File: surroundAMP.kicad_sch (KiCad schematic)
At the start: 22 parts, among them U1 NJM4580

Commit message: comments added
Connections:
- net OUPUT C L renamed OUTPUT C L
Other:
- note added: "R+L for Center Speaker Power AMP"
- note added: "R-L and L-R for rear speaker Power AMP"
- note added: "Surround Processor for rear speakers"
- note removed: "R+L for Center Speaker"
- note removed: "Surround Effector"
- moved on the sheet: R10, R11, R15, R3, R4

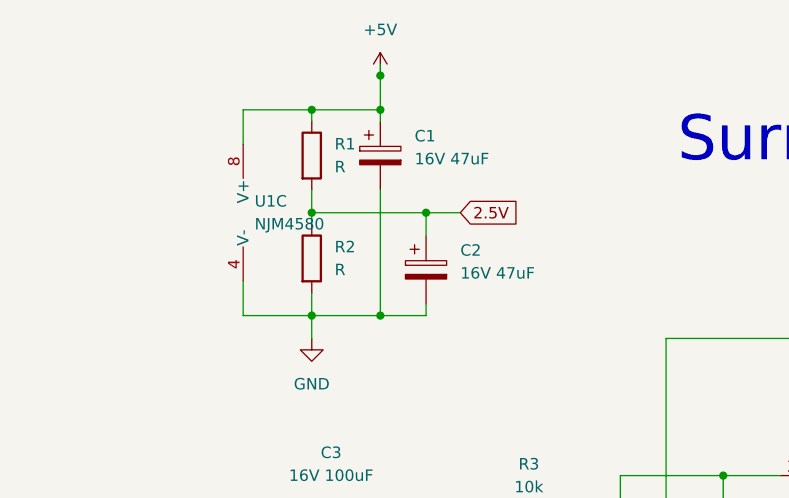
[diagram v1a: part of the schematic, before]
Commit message: resister 4.7k for 2.5V Power supply are specified
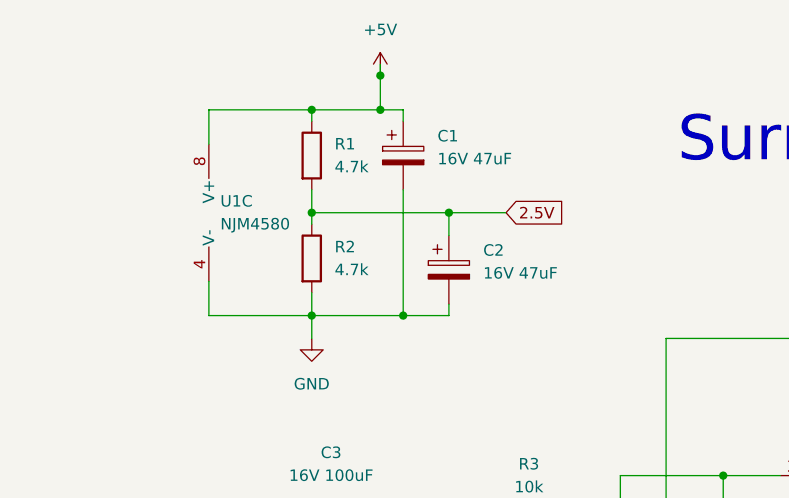
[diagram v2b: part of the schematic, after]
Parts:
- R1, R2: value R -> 4.7k
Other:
- moved on the sheet: C1, C2, U1C
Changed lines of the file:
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@@
   (junction (at 97.79 76.2) (diameter 0) (color 0 0 0 0)
   )
+  (junction (at 68.58 53.34) (diameter 0) (color 0 0 0 0)
+  )
   (junction (at 45.72 181.61) (diameter 0) (color 0 0 0 0)
   )
@@
   (junction (at 52.07 76.2) (diameter 0) (color 0 0 0 0)
   )
-  (junction (at 66.04 53.34) (diameter 0) (color 0 0 0 0)
-  )
   (junction (at 66.04 96.52) (diameter 0) (color 0 0 0 0)
   )
-  (junction (at 71.12 41.91) (diameter 0) (color 0 0 0 0)
-  )
   (junction (at 114.3 161.29) (diameter 0) (color 0 0 0 0)
   )
@@
   (junction (at 58.42 30.48) (diameter 0) (color 0 0 0 0)
   )
+  (junction (at 73.66 41.91) (diameter 0) (color 0 0 0 0)
+  )
   (junction (at 104.14 71.12) (diameter 0) (color 0 0 0 0)
   )
@@
     (stroke (width 0) (type default))
   )
-  (wire (pts (xy 66.04 53.34) (xy 71.12 53.34))
-    (stroke (width 0) (type default))
-  )
   (wire (pts (xy 46.99 96.52) (xy 46.99 172.72))
     (stroke (width 0) (type default))
@@
     (stroke (width 0) (type default))
   )
-  (wire (pts (xy 58.42 53.34) (xy 50.8 53.34))
+  (wire (pts (xy 58.42 53.34) (xy 46.99 53.34))
     (stroke (width 0) (type default))
   )
@@
     (stroke (width 0) (type default))
   )
-  (wire (pts (xy 66.04 31.75) (xy 66.04 30.48))
+  (wire (pts (xy 68.58 31.75) (xy 68.58 30.48))
     (stroke (width 0) (type default))
   )
@@
     (stroke (width 0) (type default))
   )
-  (wire (pts (xy 50.8 30.48) (xy 50.8 34.29))
+  (wire (pts (xy 46.99 30.48) (xy 46.99 34.29))
     (stroke (width 0) (type default))
   )
@@
     (stroke (width 0) (type default))
   )
-  (wire (pts (xy 58.42 41.91) (xy 71.12 41.91))
+  (wire (pts (xy 58.42 41.91) (xy 73.66 41.91))
     (stroke (width 0) (type default))
   )
@@
     (stroke (width 0) (type default))
   )
-  (wire (pts (xy 58.42 53.34) (xy 66.04 53.34))
-    (stroke (width 0) (type default))
-  )
-  (wire (pts (xy 71.12 41.91) (xy 74.93 41.91))
+  (wire (pts (xy 58.42 53.34) (xy 68.58 53.34))
     (stroke (width 0) (type default))
   )
@@
     (stroke (width 0) (type default))
   )
-  (wire (pts (xy 58.42 30.48) (xy 50.8 30.48))
+  (wire (pts (xy 58.42 30.48) (xy 46.99 30.48))
     (stroke (width 0) (type default))
   )
@@
     (stroke (width 0) (type default))
   )
+  (wire (pts (xy 73.66 41.91) (xy 80.01 41.91))
+    (stroke (width 0) (type default))
+  )
   (wire (pts (xy 140.97 171.45) (xy 129.54 171.45))
     (stroke (width 0) (type default))
@@
     (stroke (width 0) (type default))
   )
+  (wire (pts (xy 68.58 53.34) (xy 73.66 53.34))
+    (stroke (width 0) (type default))
+  )
+  (wire (pts (xy 68.58 30.48) (xy 66.04 30.48))
+    (stroke (width 0) (type default))
+  )
   (wire (pts (xy 129.54 161.29) (xy 140.97 161.29))
     (stroke (width 0) (type default))
@@
     (stroke (width 0) (type default))
   )
-  (wire (pts (xy 71.12 52.07) (xy 71.12 53.34))
+  (wire (pts (xy 73.66 52.07) (xy 73.66 53.34))
     (stroke (width 0) (type default))
   )
@@
     (stroke (width 0) (type default))
   )
-  (wire (pts (xy 66.04 39.37) (xy 66.04 53.34))
+  (wire (pts (xy 68.58 39.37) (xy 68.58 53.34))
     (stroke (width 0) (type default))
   )
@@
     (stroke (width 0) (type default))
   )
-  (wire (pts (xy 50.8 49.53) (xy 50.8 53.34))
+  (wire (pts (xy 46.99 49.53) (xy 46.99 53.34))
     (stroke (width 0) (type default))
   )
@@
     (stroke (width 0) (type default))
   )
-  (wire (pts (xy 71.12 41.91) (xy 71.12 44.45))
+  (wire (pts (xy 73.66 41.91) (xy 73.66 44.45))
     (stroke (width 0) (type default))
   )
@@
     (effects (font (size 3 3)) (justify left bottom))
   )
-  (global_label "2.5V" (shape input) (at 74.93 41.91 0) (fields_autoplaced)
+  (global_label "2.5V" (shape input) (at 80.01 41.91 0) (fields_autoplaced)
     (effects (font (size 1.27 1.27)) (justify left))
-    (property "Intersheetrefs" "${INTERSHEET_REFS}" (at 82.0276 41.91 0)
+    (property "Intersheetrefs" "${INTERSHEET_REFS}" (at 87.1076 41.91 0)
       (effects (font (size 1.27 1.27)) (justify left) hide)
     )
@@
     )
   )
-  (symbol (lib_id "Device:C_Polarized") (at 66.04 35.56 0) (unit 1)
-    (in_bom yes) (on_board yes) (dnp no) (fields_autoplaced)
-    (property "Reference" "C1" (at 69.85 33.401 0)
-      (effects (font (size 1.27 1.27)) (justify left))
-    )
-    (property "Value" "16V 47uF" (at 69.85 35.941 0)
-      (effects (font (size 1.27 1.27)) (justify left))
-    )
-    (property "Footprint" "" (at 67.0052 39.37 0)
-      (effects (font (size 1.27 1.27)) hide)
-    )
-    (property "Datasheet" "~" (at 66.04 35.56 0)
+  (symbol (lib_id "Device:C_Polarized") (at 68.58 35.56 0) (unit 1)
+    (in_bom yes) (on_board yes) (dnp no) (fields_autoplaced)
+    (property "Reference" "C1" (at 72.39 33.401 0)
+      (effects (font (size 1.27 1.27)) (justify left))
+    )
+    (property "Value" "16V 47uF" (at 72.39 35.941 0)
+      (effects (font (size 1.27 1.27)) (justify left))
+    )
+    (property "Footprint" "" (at 69.5452 39.37 0)
+      (effects (font (size 1.27 1.27)) hide)
+    )
+    (property "Datasheet" "~" (at 68.58 35.56 0)
       (effects (font (size 1.27 1.27)) hide)
     )
@@
       (effects (font (size 1.27 1.27)) (justify left))
     )
-    (property "Value" "R" (at 60.96 48.26 0)
+    (property "Value" "4.7k" (at 60.96 48.26 0)
       (effects (font (size 1.27 1.27)) (justify left))
     )
@@
     )
   )
-  (symbol (lib_id "Amplifier_Operational:NJM4580") (at 53.34 41.91 0) (unit 3)
-    (in_bom yes) (on_board yes) (dnp no) (fields_autoplaced)
-    (property "Reference" "U1" (at 52.07 40.64 0)
-      (effects (font (size 1.27 1.27)) (justify left))
-    )
-    (property "Value" "NJM4580" (at 52.07 43.18 0)
-      (effects (font (size 1.27 1.27)) (justify left))
-    )
-    (property "Footprint" "" (at 53.34 41.91 0)
-      (effects (font (size 1.27 1.27)) hide)
-    )
-    (property "Datasheet" "http://www.njr.com/semicon/PDF/NJM4580_E.pdf" (at 53.34 41.91 0)
+  (symbol (lib_id "Amplifier_Operational:NJM4580") (at 49.53 41.91 0) (unit 3)
+    (in_bom yes) (on_board yes) (dnp no) (fields_autoplaced)
+    (property "Reference" "U1" (at 48.26 40.64 0)
+      (effects (font (size 1.27 1.27)) (justify left))
+    )
+    (property "Value" "NJM4580" (at 48.26 43.18 0)
+      (effects (font (size 1.27 1.27)) (justify left))
+    )
+    (property "Footprint" "" (at 49.53 41.91 0)
+      (effects (font (size 1.27 1.27)) hide)
+    )
+    (property "Datasheet" "http://www.njr.com/semicon/PDF/NJM4580_E.pdf" (at 49.53 41.91 0)
       (effects (font (size 1.27 1.27)) hide)
     )
@@
     )
   )
-  (symbol (lib_id "Device:C_Polarized") (at 71.12 48.26 0) (unit 1)
-    (in_bom yes) (on_board yes) (dnp no) (fields_autoplaced)
-    (property "Reference" "C2" (at 74.93 46.101 0)
-      (effects (font (size 1.27 1.27)) (justify left))
-    )
-    (property "Value" "16V 47uF" (at 74.93 48.641 0)
-      (effects (font (size 1.27 1.27)) (justify left))
-    )
-    (property "Footprint" "" (at 72.0852 52.07 0)
-      (effects (font (size 1.27 1.27)) hide)
-    )
-    (property "Datasheet" "~" (at 71.12 48.26 0)
+  (symbol (lib_id "Device:C_Polarized") (at 73.66 48.26 0) (unit 1)
+    (in_bom yes) (on_board yes) (dnp no) (fields_autoplaced)
+    (property "Reference" "C2" (at 77.47 46.101 0)
+      (effects (font (size 1.27 1.27)) (justify left))
+    )
+    (property "Value" "16V 47uF" (at 77.47 48.641 0)
+      (effects (font (size 1.27 1.27)) (justify left))
+    )
+    (property "Footprint" "" (at 74.6252 52.07 0)
+      (effects (font (size 1.27 1.27)) hide)
+    )
+    (property "Datasheet" "~" (at 73.66 48.26 0)
       (effects (font (size 1.27 1.27)) hide)
     )
@@
       (effects (font (size 1.27 1.27)) (justify left))
     )
-    (property "Value" "R" (at 60.96 36.83 0)
-      (effects (font (size 1.27 1.27)) (justify left))
-    )
+    (property "Value" "4.7k" (at 60.96 36.83 0)
+      (effects (font (size 1.27 1.27)) (justify left))
+    )

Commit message: audio jack added
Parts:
- added J1: INPUT, symbol Connector_Audio:AudioJack3_Ground
- added J2: OUTPUT, symbol Connector_Audio:AudioJack3_Ground
- added J3: Center OUTPUT, symbol Connector_Audio:AudioJack3_Ground
- C3, C4: value 16V 100uF -> 16V 100uF
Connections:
- net GND: now also J1.G, J1.S, J2.G, J2.S, J3.G, J3.S
- net INPUT L: now also J1.T
- net INPUT R: now also J1.R
- net OUTPUT C L: now also J3.R, J3.T
- net OUTPUT L: now also J2.T
- net OUTPUT R: now also J2.R
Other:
- note added: "R-L signal"
- moved on the sheet: R10, R11, R13

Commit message: USB microB connector is added
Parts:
- added J4: USB_B, symbol Connector:USB_B
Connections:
- net +5V: now also J4.1 (VBUS)
- net GND: now also J4.4 (GND), J4.5 (Shield)
- no-connect marks 0 -> 2
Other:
- title: (none) -> Surround Processor for rear speakers
